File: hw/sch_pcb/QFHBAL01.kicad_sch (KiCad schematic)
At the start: 14 parts, among them J1 Conn_Coaxial, T1 ETC1-1-13, T2 ETC1-1-13

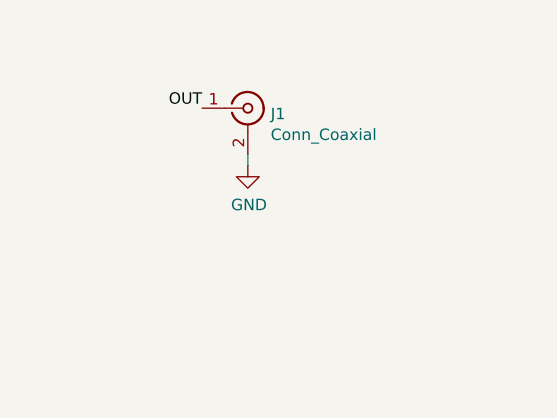
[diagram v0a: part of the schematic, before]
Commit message: Mechanical improvement.
Silkscreen clarification.
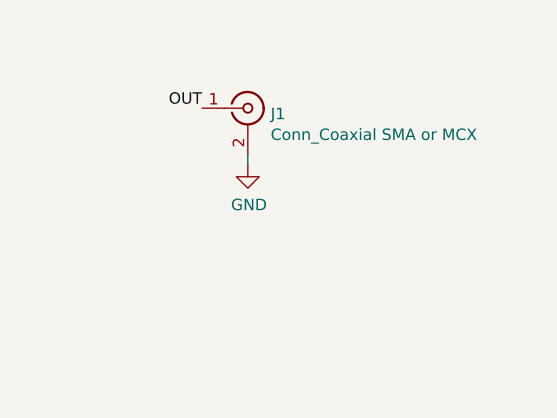
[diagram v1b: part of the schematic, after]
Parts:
- J1: value Conn_Coaxial -> Conn_Coaxial SMA or MCX
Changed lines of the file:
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@@
   (junction (at 100.965 66.675) (diameter 1.016) (color 0 0 0 0))
   (junction (at 100.965 76.835) (diameter 1.016) (color 0 0 0 0))
+  (no_connect (at 165.1 67.31))
   (no_connect (at 191.77 83.185))
-  (no_connect (at 165.1 67.31))
   (wire (pts (xy 78.74 66.675) (xy 78.74 62.865))
     (stroke (width 0) (type solid) (color 0 0 0 0))
@@
       (effects (font (size 1.27 1.27)) (justify left))
     )
-    (property "Value" "Conn_Coaxial" (id 1) (at 232.41 68.3514 0)
+    (property "Value" "Conn_Coaxial SMA or MCX" (id 1) (at 232.41 68.351 0)
       (effects (font (size 1.27 1.27)) (justify left))
     )
@@
       (effects (font (size 1.27 1.27)) hide)
     )
-    (property "Datasheet" "~" (id 3) (at 152.4 67.31 90)
+    (property "Datasheet" "https://www.minicircuits.com/pdfs/TC1-1-13MX+.pdf" (id 3) (at 152.4 67.31 90)
       (effects (font (size 1.27 1.27)) hide)
     )
@@
       (effects (font (size 1.27 1.27)) hide)
     )
-    (property "Datasheet" "~" (id 3) (at 191.77 70.485 90)
+    (property "Datasheet" "https://cdn.macom.com/datasheets/ETC1-1-13.pdf" (id 3) (at 191.77 70.485 90)
       (effects (font (size 1.27 1.27)) hide)
     )
@@
     )
     (path "/00000000-0000-0000-0000-00005f8ddcd9"
-      (reference "J1") (unit 1) (value "Conn_Coaxial") (footprint "Connector_Coaxial:SMA_Amphenol_901-144_Vertical")
+      (reference "J1") (unit 1) (value "Conn_Coaxial SMA or MCX") (footprint "Connector_Coaxial:SMA_Amphenol_901-144_Vertical")
     )
     (path "/00000000-0000-0000-0000-00005f9673c6"

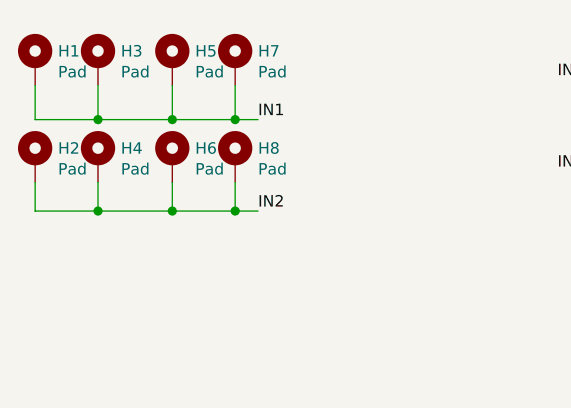
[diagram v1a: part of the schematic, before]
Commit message: Cleanup redundant pads.
Disable board clearance and unconnected vias check.
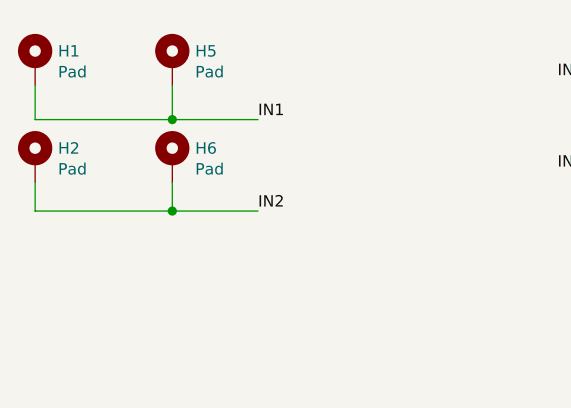
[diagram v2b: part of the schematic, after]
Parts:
- removed H3, H4, H7, H8: Pad, MountingHole:MountingHole_2.2mm_M2_Pad, symbol Mechanical:MountingHole_Pad
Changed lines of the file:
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@@
   (page 1 1)
   (paper "A4")
-  (junction (at 85.725 66.675) (diameter 1.016) (color 0 0 0 0))
-  (junction (at 85.725 76.835) (diameter 1.016) (color 0 0 0 0))
   (junction (at 93.98 66.675) (diameter 1.016) (color 0 0 0 0))
   (junction (at 93.98 76.835) (diameter 1.016) (color 0 0 0 0))
-  (junction (at 100.965 66.675) (diameter 1.016) (color 0 0 0 0))
-  (junction (at 100.965 76.835) (diameter 1.016) (color 0 0 0 0))
+  (no_connect (at 191.77 83.185))
   (no_connect (at 165.1 67.31))
-  (no_connect (at 191.77 83.185))
   (wire (pts (xy 78.74 66.675) (xy 78.74 62.865))
     (stroke (width 0) (type solid) (color 0 0 0 0))
   )
+  (wire (pts (xy 78.74 66.675) (xy 93.98 66.675))
+    (stroke (width 0) (type solid) (color 0 0 0 0))
+  )
   (wire (pts (xy 78.74 76.835) (xy 78.74 73.66))
     (stroke (width 0) (type solid) (color 0 0 0 0))
   )
-  (wire (pts (xy 85.725 66.675) (xy 78.74 66.675))
-    (stroke (width 0) (type solid) (color 0 0 0 0))
-  )
-  (wire (pts (xy 85.725 66.675) (xy 85.725 62.865))
-    (stroke (width 0) (type solid) (color 0 0 0 0))
-  )
-  (wire (pts (xy 85.725 76.835) (xy 78.74 76.835))
-    (stroke (width 0) (type solid) (color 0 0 0 0))
-  )
-  (wire (pts (xy 85.725 76.835) (xy 85.725 73.66))
-    (stroke (width 0) (type solid) (color 0 0 0 0))
-  )
-  (wire (pts (xy 93.98 66.675) (xy 85.725 66.675))
+  (wire (pts (xy 78.74 76.835) (xy 93.98 76.835))
     (stroke (width 0) (type solid) (color 0 0 0 0))
   )
@@
     (stroke (width 0) (type solid) (color 0 0 0 0))
   )
-  (wire (pts (xy 93.98 76.835) (xy 85.725 76.835))
+  (wire (pts (xy 93.98 66.675) (xy 103.505 66.675))
     (stroke (width 0) (type solid) (color 0 0 0 0))
   )
@@
     (stroke (width 0) (type solid) (color 0 0 0 0))
   )
-  (wire (pts (xy 100.965 62.865) (xy 100.965 66.675))
-    (stroke (width 0) (type solid) (color 0 0 0 0))
-  )
-  (wire (pts (xy 100.965 66.675) (xy 93.98 66.675))
-    (stroke (width 0) (type solid) (color 0 0 0 0))
-  )
-  (wire (pts (xy 100.965 66.675) (xy 103.505 66.675))
-    (stroke (width 0) (type solid) (color 0 0 0 0))
-  )
-  (wire (pts (xy 100.965 76.835) (xy 93.98 76.835))
-    (stroke (width 0) (type solid) (color 0 0 0 0))
-  )
-  (wire (pts (xy 100.965 76.835) (xy 100.965 73.66))
-    (stroke (width 0) (type solid) (color 0 0 0 0))
-  )
-  (wire (pts (xy 100.965 76.835) (xy 103.505 76.835))
+  (wire (pts (xy 93.98 76.835) (xy 103.505 76.835))
     (stroke (width 0) (type solid) (color 0 0 0 0))
   )
@@
     )
   )
-  (symbol (lib_id "Mechanical:MountingHole_Pad") (at 85.725 60.325 0) (unit 1)
-    (in_bom yes) (on_board yes)
-    (property "Reference" "H3" (id 0) (at 88.265 59.0804 0)
-      (effects (font (size 1.27 1.27)) (justify left))
-    )
-    (property "Value" "Pad" (id 1) (at 88.265 61.3918 0)
-      (effects (font (size 1.27 1.27)) (justify left))
-    )
-    (property "Footprint" "MountingHole:MountingHole_2.2mm_M2_Pad" (id 2) (at 85.725 60.325 0)
-      (effects (font (size 1.27 1.27)) hide)
-    )
-    (property "Datasheet" "~" (id 3) (at 85.725 60.325 0)
-      (effects (font (size 1.27 1.27)) hide)
-    )
-  )
-  (symbol (lib_id "Mechanical:MountingHole_Pad") (at 85.725 71.12 0) (unit 1)
-    (in_bom yes) (on_board yes)
-    (property "Reference" "H4" (id 0) (at 88.265 69.8754 0)
-      (effects (font (size 1.27 1.27)) (justify left))
-    )
-    (property "Value" "Pad" (id 1) (at 88.265 72.1868 0)
-      (effects (font (size 1.27 1.27)) (justify left))
-    )
-    (property "Footprint" "MountingHole:MountingHole_2.2mm_M2_Pad" (id 2) (at 85.725 71.12 0)
-      (effects (font (size 1.27 1.27)) hide)
-    )
-    (property "Datasheet" "~" (id 3) (at 85.725 71.12 0)
-      (effects (font (size 1.27 1.27)) hide)
-    )
-  )
   (symbol (lib_id "Mechanical:MountingHole_Pad") (at 93.98 60.325 0) (unit 1)
     (in_bom yes) (on_board yes)
@@
     )
     (property "Datasheet" "~" (id 3) (at 93.98 71.12 0)
-      (effects (font (size 1.27 1.27)) hide)
-    )
-  )
-  (symbol (lib_id "Mechanical:MountingHole_Pad") (at 100.965 60.325 0) (unit 1)
-    (in_bom yes) (on_board yes)
-    (property "Reference" "H7" (id 0) (at 103.505 59.0804 0)
-      (effects (font (size 1.27 1.27)) (justify left))
-    )
-    (property "Value" "Pad" (id 1) (at 103.505 61.3918 0)
-      (effects (font (size 1.27 1.27)) (justify left))
-    )
-    (property "Footprint" "MountingHole:MountingHole_2.2mm_M2_Pad" (id 2) (at 100.965 60.325 0)
-      (effects (font (size 1.27 1.27)) hide)
-    )
-    (property "Datasheet" "~" (id 3) (at 100.965 60.325 0)
-      (effects (font (size 1.27 1.27)) hide)
-    )
-  )
-  (symbol (lib_id "Mechanical:MountingHole_Pad") (at 100.965 71.12 0) (unit 1)
-    (in_bom yes) (on_board yes)
-    (property "Reference" "H8" (id 0) (at 103.505 69.8754 0)
-      (effects (font (size 1.27 1.27)) (justify left))
-    )
-    (property "Value" "Pad" (id 1) (at 103.505 72.1868 0)
-      (effects (font (size 1.27 1.27)) (justify left))
-    )
-    (property "Footprint" "MountingHole:MountingHole_2.2mm_M2_Pad" (id 2) (at 100.965 71.12 0)
-      (effects (font (size 1.27 1.27)) hide)
-    )
-    (property "Datasheet" "~" (id 3) (at 100.965 71.12 0)
       (effects (font (size 1.27 1.27)) hide)
     )
@@
       (reference "H2") (unit 1) (value "Pad") (footprint "MountingHole:MountingHole_2.2mm_M2_Pad")
     )
-    (path "/00000000-0000-0000-0000-00005f8db409"
-      (reference "H3") (unit 1) (value "Pad") (footprint "MountingHole:MountingHole_2.2mm_M2_Pad")
-    )
-    (path "/00000000-0000-0000-0000-00005f9621ff"
-      (reference "H4") (unit 1) (value "Pad") (footprint "MountingHole:MountingHole_2.2mm_M2_Pad")
-    )
     (path "/00000000-0000-0000-0000-00005f8dc703"
       (reference "H5") (unit 1) (value "Pad") (footprint "MountingHole:MountingHole_2.2mm_M2_Pad")
@@
       (reference "H6") (unit 1) (value "Pad") (footprint "MountingHole:MountingHole_2.2mm_M2_Pad")
     )
-    (path "/00000000-0000-0000-0000-00005f8dc6f9"
-      (reference "H7") (unit 1) (value "Pad") (footprint "MountingHole:MountingHole_2.2mm_M2_Pad")
-    )
-    (path "/00000000-0000-0000-0000-00005f962213"
-      (reference "H8") (unit 1) (value "Pad") (footprint "MountingHole:MountingHole_2.2mm_M2_Pad")
-    )
     (path "/00000000-0000-0000-0000-00005f959145"
